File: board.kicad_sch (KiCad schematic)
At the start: 6 parts, among them U1 MC68060RC50, U2 XC95144XL-5TQG100C, U3 SST39VF1601C-70-4C-EKE, U4 IS61WV51216BLL-10TLI, U5 IS61WV51216BLL-10TLI, U6 SST39VF1601C-70-4C-EKE

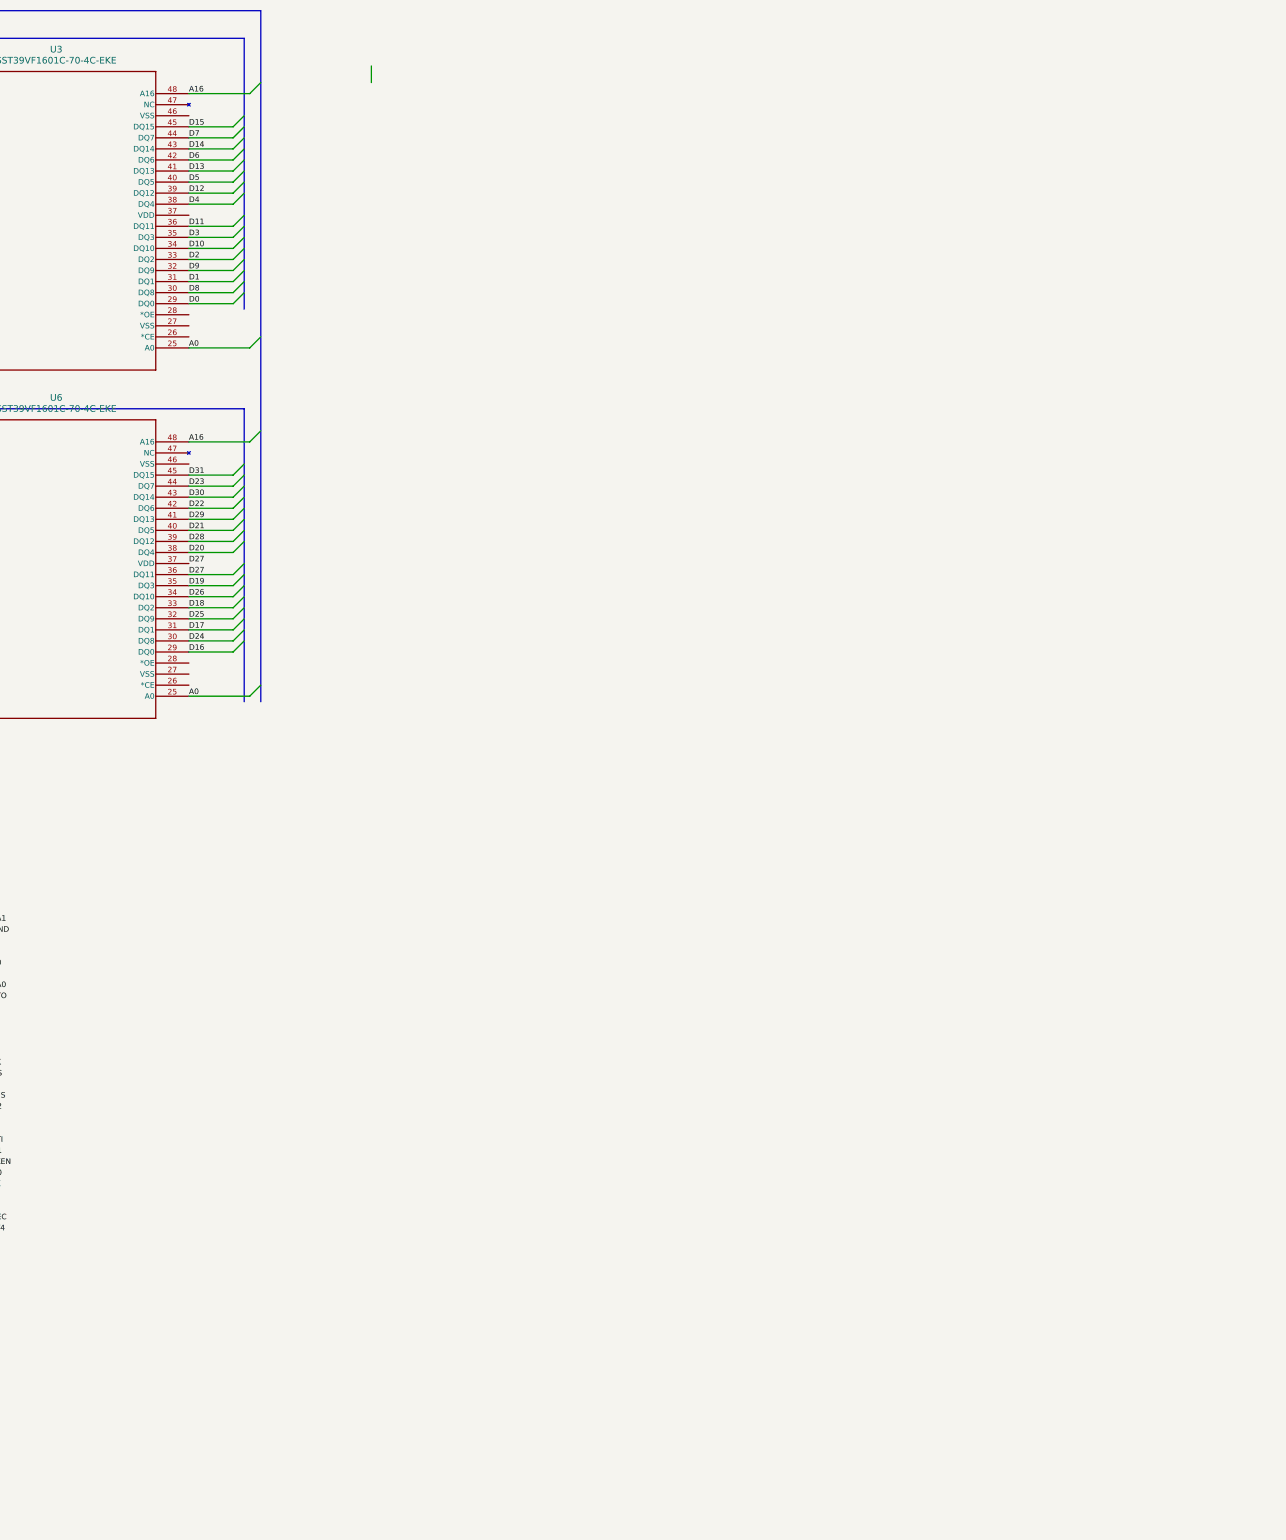
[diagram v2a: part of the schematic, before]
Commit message: Added buffers and re-rationalised traces
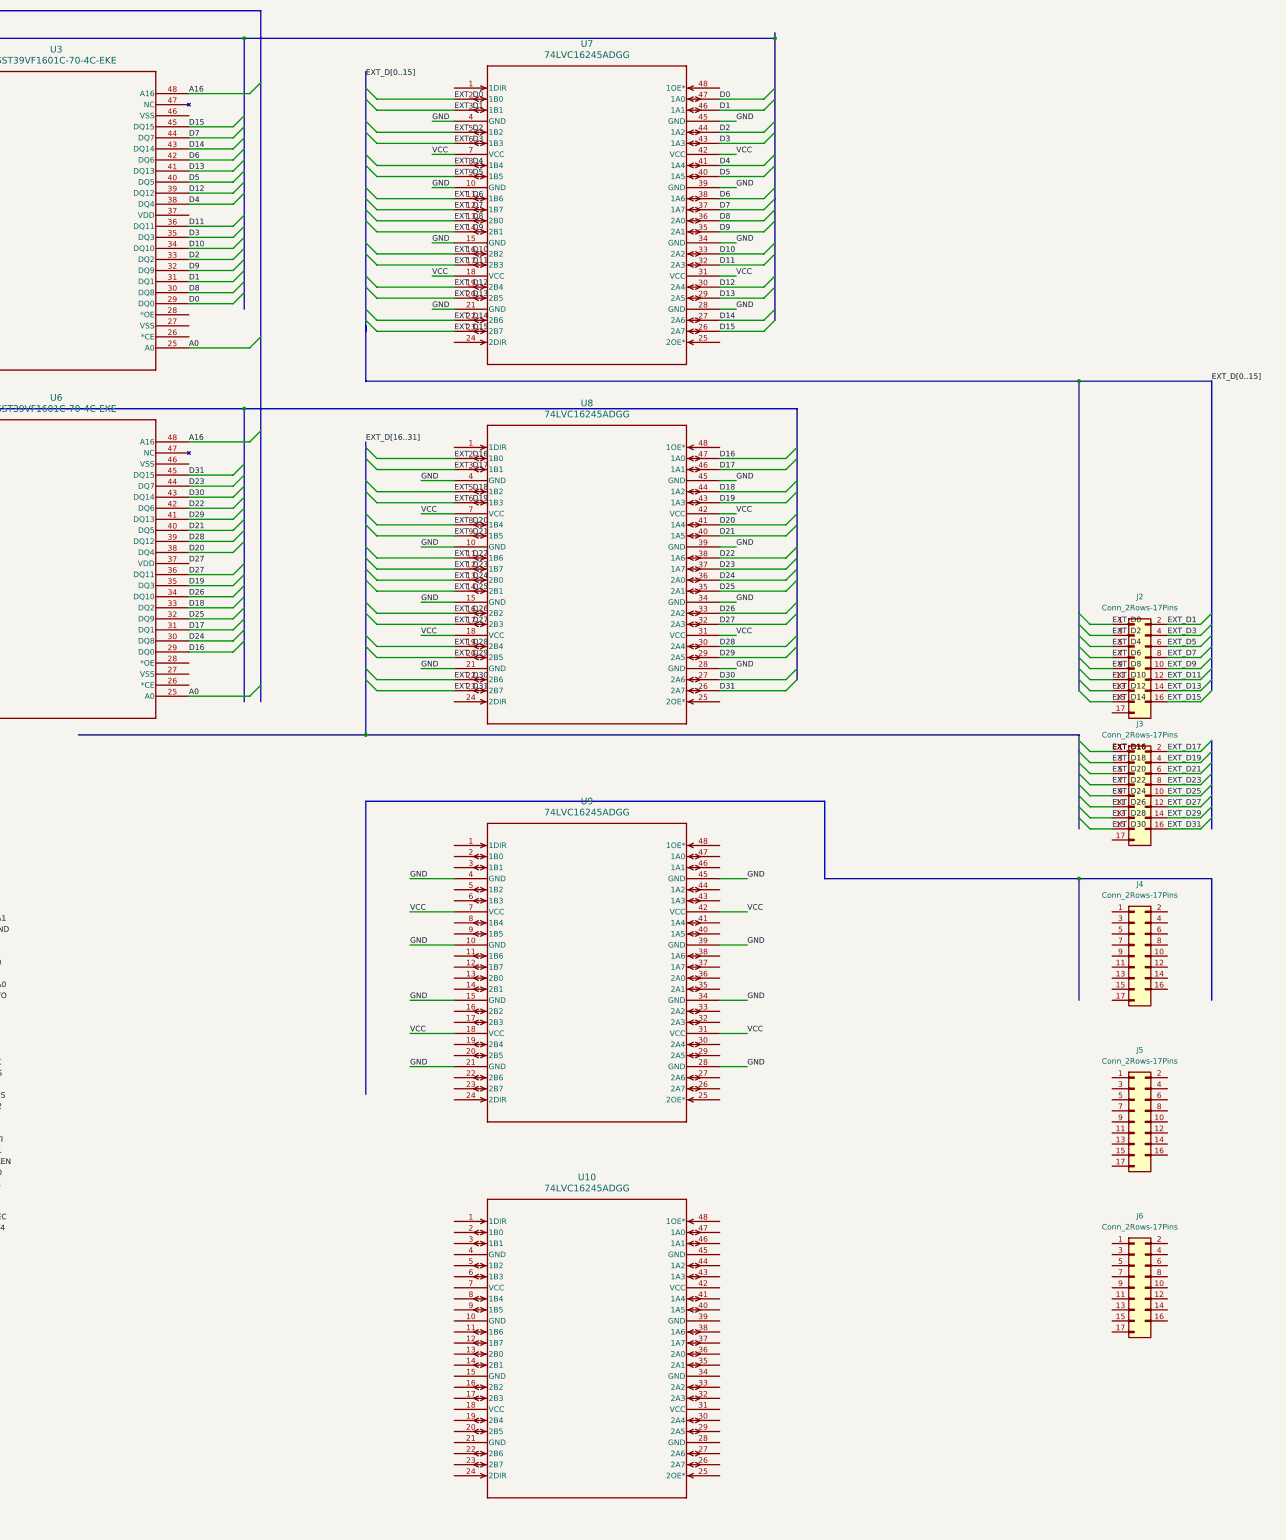
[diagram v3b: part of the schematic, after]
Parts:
- added J2, J3, J4, J5, J6: Conn_2Rows-17Pins, symbol Connector_Generic:Conn_2Rows-17Pins
- added U10, U7, U8, U9: 74LVC16245ADGG, SOT362-1_NEX, symbol 7416254 buffer:74LVC16245ADGG
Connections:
- net D0: now also U7.47 (1A0)
- net D1: now also U7.46 (1A1)
- net D10: now also U7.33 (2A2)
- net D11: now also U7.32 (2A3)
- net D12: now also U7.30 (2A4)
- net D13: now also U7.29 (2A5)
- net D14: now also U7.27 (2A6)
- net D15: now also U7.26 (2A7)
- net D16: now also U8.47 (1A0)
- net D17: now also U8.46 (1A1)
- net D18: now also U8.44 (1A2)
- net D19: now also U8.43 (1A3)
- net D2: now also U7.44 (1A2)
- net D20: now also U8.41 (1A4)
- net D21: now also U8.40 (1A5)
- net D22: now also U8.38 (1A6)
- net D23: now also U8.37 (1A7)
- net D24: now also U8.36 (2A0)
- net D25: now also U8.35 (2A1)
- net D26: now also U8.33 (2A2)
- net D27: now also U8.32 (2A3)
- net D28: now also U8.30 (2A4)
- net D29: now also U8.29 (2A5)
- net D3: now also U7.43 (1A3)
- net D30: now also U8.27 (2A6)
- net D31: now also U8.26 (2A7)
- net D4: now also U7.41 (1A4)
- net D5: now also U7.40 (1A5)
- net D6: now also U7.38 (1A6)
- net D7: now also U7.37 (1A7)
- net D8: now also U7.36 (2A0)
- net D9: now also U7.35 (2A1)
- net GND: now also U7.10 (GND), U7.15 (GND), U7.21 (GND), U7.28 (GND), U7.34 (GND), U7.39 (GND), U7.4 (GND), U7.45 (GND), U8.10 (GND), U8.15 (GND), U8.21 (GND), U8.28 (GND), U8.34 (GND), U8.39 (GND), U8.4 (GND), U8.45 (GND), U9.10 (GND), U9.15 (GND), U9.21 (GND), U9.28 (GND), U9.34 (GND), U9.39 (GND), U9.4 (GND), U9.45 (GND)
- net VCC: now also U7.18 (VCC), U7.31 (VCC), U7.42 (VCC), U7.7 (VCC), U8.18 (VCC), U8.31 (VCC), U8.42 (VCC), U8.7 (VCC), U9.18 (VCC), U9.31 (VCC), U9.42 (VCC), U9.7 (VCC)
- new net EXT_D0: J2.1 (Pin_1), U7.2 (1B0)
- new net EXT_D1: J2.2 (Pin_2), U7.3 (1B1)
- new net EXT_D10: J2.11 (Pin_11), U7.16 (2B2)
- new net EXT_D11: J2.12 (Pin_12), U7.17 (2B3)
- new net EXT_D12: J2.13 (Pin_13), U7.19 (2B4)
- new net EXT_D13: J2.14 (Pin_14), U7.20 (2B5)
- new net EXT_D14: J2.15 (Pin_15), U7.22 (2B6)
- new net EXT_D15: J2.16 (Pin_16), U7.23 (2B7)
- new net EXT_D16: J3.1 (Pin_1), U8.2 (1B0)
- new net EXT_D17: J3.2 (Pin_2), U8.3 (1B1)
- new net EXT_D18: J3.3 (Pin_3), U8.5 (1B2)
- new net EXT_D19: J3.4 (Pin_4), U8.6 (1B3)
- new net EXT_D2: J2.3 (Pin_3), U7.5 (1B2)
- new net EXT_D20: J3.5 (Pin_5), U8.8 (1B4)
- new net EXT_D21: J3.6 (Pin_6), U8.9 (1B5)
- new net EXT_D22: J3.7 (Pin_7), U8.11 (1B6)
- new net EXT_D23: J3.8 (Pin_8), U8.12 (1B7)
- new net EXT_D24: J3.9 (Pin_9), U8.13 (2B0)
- new net EXT_D25: J3.10 (Pin_10), U8.14 (2B1)
- new net EXT_D26: J3.11 (Pin_11), U8.16 (2B2)
- new net EXT_D27: J3.12 (Pin_12), U8.17 (2B3)
- new net EXT_D28: J3.13 (Pin_13), U8.19 (2B4)
- new net EXT_D29: J3.14 (Pin_14), U8.20 (2B5)
- new net EXT_D3: J2.4 (Pin_4), U7.6 (1B3)
- new net EXT_D30: J3.15 (Pin_15), U8.22 (2B6)
- new net EXT_D31: J3.16 (Pin_16), U8.23 (2B7)
- new net EXT_D4: J2.5 (Pin_5), U7.8 (1B4)
- new net EXT_D5: J2.6 (Pin_6), U7.9 (1B5)
- new net EXT_D6: J2.7 (Pin_7), U7.11 (1B6)
- new net EXT_D7: J2.8 (Pin_8), U7.12 (1B7)
- new net EXT_D8: J2.9 (Pin_9), U7.13 (2B0)
- new net EXT_D9: J2.10 (Pin_10), U7.14 (2B1)

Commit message: Added jumpers for expansion board and more address lines to the CPLD
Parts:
- removed J6: Conn_2Rows-17Pins, symbol Connector_Generic:Conn_2Rows-17Pins
- J2, J3, J4, J5: value Conn_2Rows-17Pins -> Conn_2Rows-33Pins; footprint (none) -> Connector_PinHeader_2.54mm:PinHeader_2x17_P2.54mm_Vertical; symbol Connector_Generic:Conn_2Rows-17Pins -> Connector_Generic:Conn_2Rows-33Pins
- U10, U7, U8, U9: value 74LVC16245ADGG -> 74LVC162245ADGG
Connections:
- net A0: now also U9.47 (1A0)
- net A1: now also U9.46 (1A1)
- net A10: now also U9.33 (2A2)
- net A11: now also U9.32 (2A3)
- net A12: now also U9.30 (2A4)
- net A13: now also U9.29 (2A5)
- net A14: now also U2.89 (NC), U9.27 (2A6)
- net A15: now also U2.90 (NC), U9.26 (2A7)
- net A16: now also U10.26 (2A7), U2.91 (NC)
- net A17: now also U10.27 (2A6), U2.92 (NC)
- net A18: now also U10.29 (2A5), U2.93 (NC); no longer U2.89 (NC)
- net A19: now also U10.30 (2A4), U2.94 (IO); no longer U2.90 (NC)
- net A2: now also U9.44 (1A2)
- net A20: now also U10.32 (2A3), U2.95 (IO); no longer U2.91 (NC)
- net A21: now also U10.33 (2A2), U2.96 (IO); no longer U2.92 (NC)
- net A22: now also U10.35 (2A1), U2.97 (IO); no longer U2.93 (NC)
- net A23: now also U10.36 (2A0), U2.1 (I/O/GTS3)
- net A24: now also U10.37 (1A7), U2.2 (I/O/GTS4)
- net A25: now also U10.38 (1A6), U2.3 (I/O/GTS1)
- net A26: now also U10.40 (1A5), U2.4 (I/O/GTS2)
- net A27: now also U10.41 (1A4), U2.6 (IO)
- net A28: now also U10.43 (1A3), U2.7 (IO)
- net A29: now also U10.44 (1A2), U2.8 (IO)
- net A3: now also U9.43 (1A3)
- net A30: now also U10.46 (1A1), U2.9 (IO)
- net A31: now also U10.47 (1A0), U2.10 (IO)
- net A4: now also U9.41 (1A4)
- net A5: now also U9.40 (1A5)
- net A6: now also U9.38 (1A6)
- net A7: now also U9.37 (1A7)
- net A8: now also U9.36 (2A0)
- net A9: now also U9.35 (2A1)
- net EXT_D0: now also J2.2 (Pin_2); no longer J2.1 (Pin_1)
- net EXT_D1: now also J2.4 (Pin_4); no longer J2.2 (Pin_2)
- net EXT_D10: now also J2.22 (Pin_22); no longer J2.11 (Pin_11)
- net EXT_D11: now also J2.24 (Pin_24); no longer J2.12 (Pin_12)
- net EXT_D12: now also J2.26 (Pin_26); no longer J2.13 (Pin_13)
- net EXT_D13: now also J2.28 (Pin_28); no longer J2.14 (Pin_14)
- net EXT_D14: now also J2.30 (Pin_30); no longer J2.15 (Pin_15)
- net EXT_D15: now also J2.32 (Pin_32); no longer J2.16 (Pin_16)
- net EXT_D16: now also J3.2 (Pin_2); no longer J3.1 (Pin_1)
- net EXT_D17: now also J3.4 (Pin_4); no longer J3.2 (Pin_2)
- net EXT_D18: now also J3.6 (Pin_6); no longer J3.3 (Pin_3)
- net EXT_D19: now also J3.8 (Pin_8); no longer J3.4 (Pin_4)
- net EXT_D2: now also J2.6 (Pin_6); no longer J2.3 (Pin_3)
- net EXT_D20: now also J3.10 (Pin_10); no longer J3.5 (Pin_5)
- net EXT_D21: now also J3.12 (Pin_12); no longer J3.6 (Pin_6)
- net EXT_D22: now also J3.14 (Pin_14); no longer J3.7 (Pin_7)
- net EXT_D23: now also J3.16 (Pin_16); no longer J3.8 (Pin_8)
- net EXT_D24: now also J3.18 (Pin_18); no longer J3.9 (Pin_9)
- net EXT_D25: now also J3.20 (Pin_20); no longer J3.10 (Pin_10)
- net EXT_D26: now also J3.22 (Pin_22); no longer J3.11 (Pin_11)
- net EXT_D27: now also J3.24 (Pin_24); no longer J3.12 (Pin_12)
- net EXT_D28: now also J3.26 (Pin_26); no longer J3.13 (Pin_13)
- net EXT_D29: now also J3.28 (Pin_28); no longer J3.14 (Pin_14)
- net EXT_D3: now also J2.8 (Pin_8); no longer J2.4 (Pin_4)
- net EXT_D30: now also J3.30 (Pin_30); no longer J3.15 (Pin_15)
- net EXT_D31: now also J3.32 (Pin_32); no longer J3.16 (Pin_16)
- net EXT_D4: now also J2.10 (Pin_10); no longer J2.5 (Pin_5)
- net EXT_D5: now also J2.12 (Pin_12); no longer J2.6 (Pin_6)
- net EXT_D6: now also J2.14 (Pin_14); no longer J2.7 (Pin_7)
- net EXT_D7: now also J2.16 (Pin_16); no longer J2.8 (Pin_8)
- net EXT_D8: now also J2.18 (Pin_18); no longer J2.9 (Pin_9)
- net EXT_D9: now also J2.20 (Pin_20); no longer J2.10 (Pin_10)
- net GND: now also J2.1 (Pin_1), J2.11 (Pin_11), J2.13 (Pin_13), J2.15 (Pin_15), J2.17 (Pin_17), J2.19 (Pin_19), J2.21 (Pin_21), J2.23 (Pin_23), J2.25 (Pin_25), J2.27 (Pin_27), J2.29 (Pin_29), J2.3 (Pin_3), J2.31 (Pin_31), J2.33 (Pin_33), J2.5 (Pin_5), J2.7 (Pin_7), J2.9 (Pin_9), J3.1 (Pin_1), J3.11 (Pin_11), J3.13 (Pin_13), J3.15 (Pin_15), J3.17 (Pin_17), J3.19 (Pin_19), J3.21 (Pin_21), J3.23 (Pin_23), J3.25 (Pin_25), J3.27 (Pin_27), J3.29 (Pin_29), J3.3 (Pin_3), J3.31 (Pin_31), J3.33 (Pin_33), J3.5 (Pin_5), J3.7 (Pin_7), J3.9 (Pin_9), J4.1 (Pin_1), J4.11 (Pin_11), J4.13 (Pin_13), J4.15 (Pin_15), J4.17 (Pin_17), J4.19 (Pin_19), J4.21 (Pin_21), J4.23 (Pin_23), J4.25 (Pin_25), J4.27 (Pin_27), J4.29 (Pin_29), J4.3 (Pin_3), J4.31 (Pin_31), J4.33 (Pin_33), J4.5 (Pin_5), J4.7 (Pin_7), J4.9 (Pin_9), J5.1 (Pin_1), J5.11 (Pin_11), J5.13 (Pin_13), J5.15 (Pin_15), J5.17 (Pin_17), J5.19 (Pin_19), J5.21 (Pin_21), J5.23 (Pin_23), J5.25 (Pin_25), J5.27 (Pin_27), J5.29 (Pin_29), J5.3 (Pin_3), J5.31 (Pin_31), J5.33 (Pin_33), J5.5 (Pin_5), J5.7 (Pin_7), J5.9 (Pin_9), U2.100 (GND), U2.21 (GND), U2.31 (GND), U2.44 (GND), U2.62 (GND), U2.69 (GND), U2.75 (GND), U2.84 (GND)
- net VCC: now also U2.26 (VCCIO2.5V/3.3V), U2.38 (VCCIO2.5V/3.3V), U2.5 (VCCINT3.3V), U2.51 (VCCIO2.5V/3.3V), U2.57 (VCCINT3.3V), U2.88 (VCCIO2.5V/3.3V), U2.98 (VCCINT3.3V)
- net EXT_A27: now reaches J5.10 (Pin_10)
- net EXT_A27: now also U10.8 (1B4)
- net EXT_A26: now reaches J5.12 (Pin_12)
- net EXT_A26: now also U10.9 (1B5)
- net EXT_A25: now reaches J5.14 (Pin_14)
- net EXT_A25: now also U10.11 (1B6)
- net EXT_A24: now reaches J5.16 (Pin_16)
- net EXT_A24: now also U10.12 (1B7)
- net EXT_A31: now reaches J5.2 (Pin_2)
- net EXT_A31: now also U10.2 (1B0)
- net EXT_A30: now reaches J5.4 (Pin_4)
- net EXT_A30: now also U10.3 (1B1)
- net EXT_A29: now reaches J5.6 (Pin_6)
- net EXT_A29: now also U10.5 (1B2)
- net EXT_A28: now reaches J5.8 (Pin_8)
- net EXT_A28: now also U10.6 (1B3)
- net EXT_A6: now reaches U9.11 (1B6)
- net EXT_A6: now also J4.14 (Pin_14)
- net EXT_A7: now reaches U9.12 (1B7)
- net EXT_A7: now also J4.16 (Pin_16)
- net EXT_A8: now reaches U9.13 (2B0)
- net EXT_A8: now also J4.18 (Pin_18)
- net EXT_A9: now reaches U9.14 (2B1)
- net EXT_A9: now also J4.20 (Pin_20)
- net EXT_A10: now reaches U9.16 (2B2)
- net EXT_A10: now also J4.22 (Pin_22)
- net EXT_A11: now reaches U9.17 (2B3)
- net EXT_A11: now also J4.24 (Pin_24)
- net EXT_A12: now reaches U9.19 (2B4)
- net EXT_A12: now also J4.26 (Pin_26)
- net EXT_A0: now reaches U9.2 (1B0)
- net EXT_A0: now also J4.2 (Pin_2)
- net EXT_A13: now reaches U9.20 (2B5)
- net EXT_A13: now also J4.28 (Pin_28)
- net EXT_A14: now reaches U9.22 (2B6)
- net EXT_A14: now also J4.30 (Pin_30)
- net EXT_A15: now reaches U9.23 (2B7)
- net EXT_A15: now also J4.32 (Pin_32)
- net EXT_A1: now reaches U9.3 (1B1)
- net EXT_A1: now also J4.4 (Pin_4)
- net EXT_A2: now reaches U9.5 (1B2)
- net EXT_A2: now also J4.6 (Pin_6)
- net EXT_A3: now reaches U9.6 (1B3)
- net EXT_A3: now also J4.8 (Pin_8)
- net EXT_A4: now reaches U9.8 (1B4)
- net EXT_A4: now also J4.10 (Pin_10)
- net EXT_A5: now reaches U9.9 (1B5)
- net EXT_A5: now also J4.12 (Pin_12)
- net EXT_A23: now reaches U10.13 (2B0)
- net EXT_A23: now also J5.18 (Pin_18)
- net EXT_A22: now reaches U10.14 (2B1)
- net EXT_A22: now also J5.20 (Pin_20)
- net EXT_A21: now reaches U10.16 (2B2)
- net EXT_A21: now also J5.22 (Pin_22)
- net EXT_A20: now reaches U10.17 (2B3)
- net EXT_A20: now also J5.24 (Pin_24)
- net EXT_A19: now reaches U10.19 (2B4)
- net EXT_A19: now also J5.26 (Pin_26)
- net EXT_A18: now reaches U10.20 (2B5)
- net EXT_A18: now also J5.28 (Pin_28)
- net EXT_A17: now reaches U10.22 (2B6)
- net EXT_A17: now also J5.30 (Pin_30)
- net EXT_A16: now reaches U10.23 (2B7)
- net EXT_A16: now also J5.32 (Pin_32)

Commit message: Added ROM and RAM control signals
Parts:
- added J6: Conn_2Rows-33Pins, Connector_PinHeader_2.54mm:PinHeader_2x17_P2.54mm_Vertical, symbol Connector_Generic:Conn_2Rows-33Pins
- added U11: 74LVC162245ADGG, SOT362-1_NEX, symbol 7416254 buffer:74LVC16245ADGG
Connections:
- net BS0: now also U5.40 (*UB)
- net BS1: now also U5.39 (*LB)
- net BS2: now also U4.40 (*UB)
- net BS3: now also U4.39 (*LB)
- net D27: no longer U6.37 (VDD)
- net GND: now also U3.27 (VSS), U3.46 (VSS), U4.12 (GND), U4.34 (GND), U5.12 (GND), U5.34 (GND), U6.27 (VSS), U6.46 (VSS)
- net U1C-CLA: now also U2.47 (IO); no longer U2.39 (IO)
- net U1C-PST0: now also U2.52 (IO); no longer U2.45 (TDI)
- net U1C-PST1: now also U2.54 (IO); no longer U2.47 (IO)
- net U1C-PST2: now also U2.56 (IO); no longer U2.49 (IO)
- net U1C-PST3: now also U2.49 (IO); no longer U2.41 (IO)
- net U1C-RW: now also U2.50 (IO); no longer U2.43 (IO)
- net U1C-SAS: now also U2.58 (NC); no longer U2.50 (IO)
- net U1C-SIZ0: no longer U2.37 (IO)
- net U1C-SIZ1: no longer U2.42 (IO)
- net U1C-TA: now also U2.55 (IO); no longer U2.48 (IO)
- net U1C-TIP: now also U2.53 (IO); no longer U2.46 (IO)
- net U1C-TM0: now also U2.45 (TDI); no longer U2.35 (IO)
- net U1C-TM1: now also U2.43 (IO); no longer U2.34 (IO)
- net U1C-TM2: now also U2.46 (IO); no longer U2.36 (IO)
- net U1C-TS: now also U2.48 (IO); no longer U2.40 (IO)
- net VCC: now also U3.37 (VDD), U4.11 (VDD), U4.33 (VDD), U5.11 (VDD), U5.33 (VDD), U6.37 (VDD)
- net RW: now reaches U6.11 (*WE)
- net RW: now also U2.37 (IO), U3.11 (*WE), U4.17 (*WE), U5.17 (*WE)
- net EPROM_CS: now reaches U6.26 (*CE)
- net EPROM_CS: now also U2.41 (IO), U3.26 (*CE)
- net EPROM_OE: now reaches U6.28 (*OE)
- net EPROM_OE: now also U2.42 (IO), U3.28 (*OE)
- net RAM_OE: now reaches U4.41 (*OE)
- net RAM_OE: now also U2.40 (IO), U5.41 (*OE)
- net RAM_CS: now reaches U4.6 (*CE)
- net RAM_CS: now also U2.39 (IO), U5.6 (*CE)
